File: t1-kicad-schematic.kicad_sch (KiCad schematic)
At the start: 7 parts, among them SW1 SW_MEC_5G, SW2 SW_MEC_5G, U1 Keypad

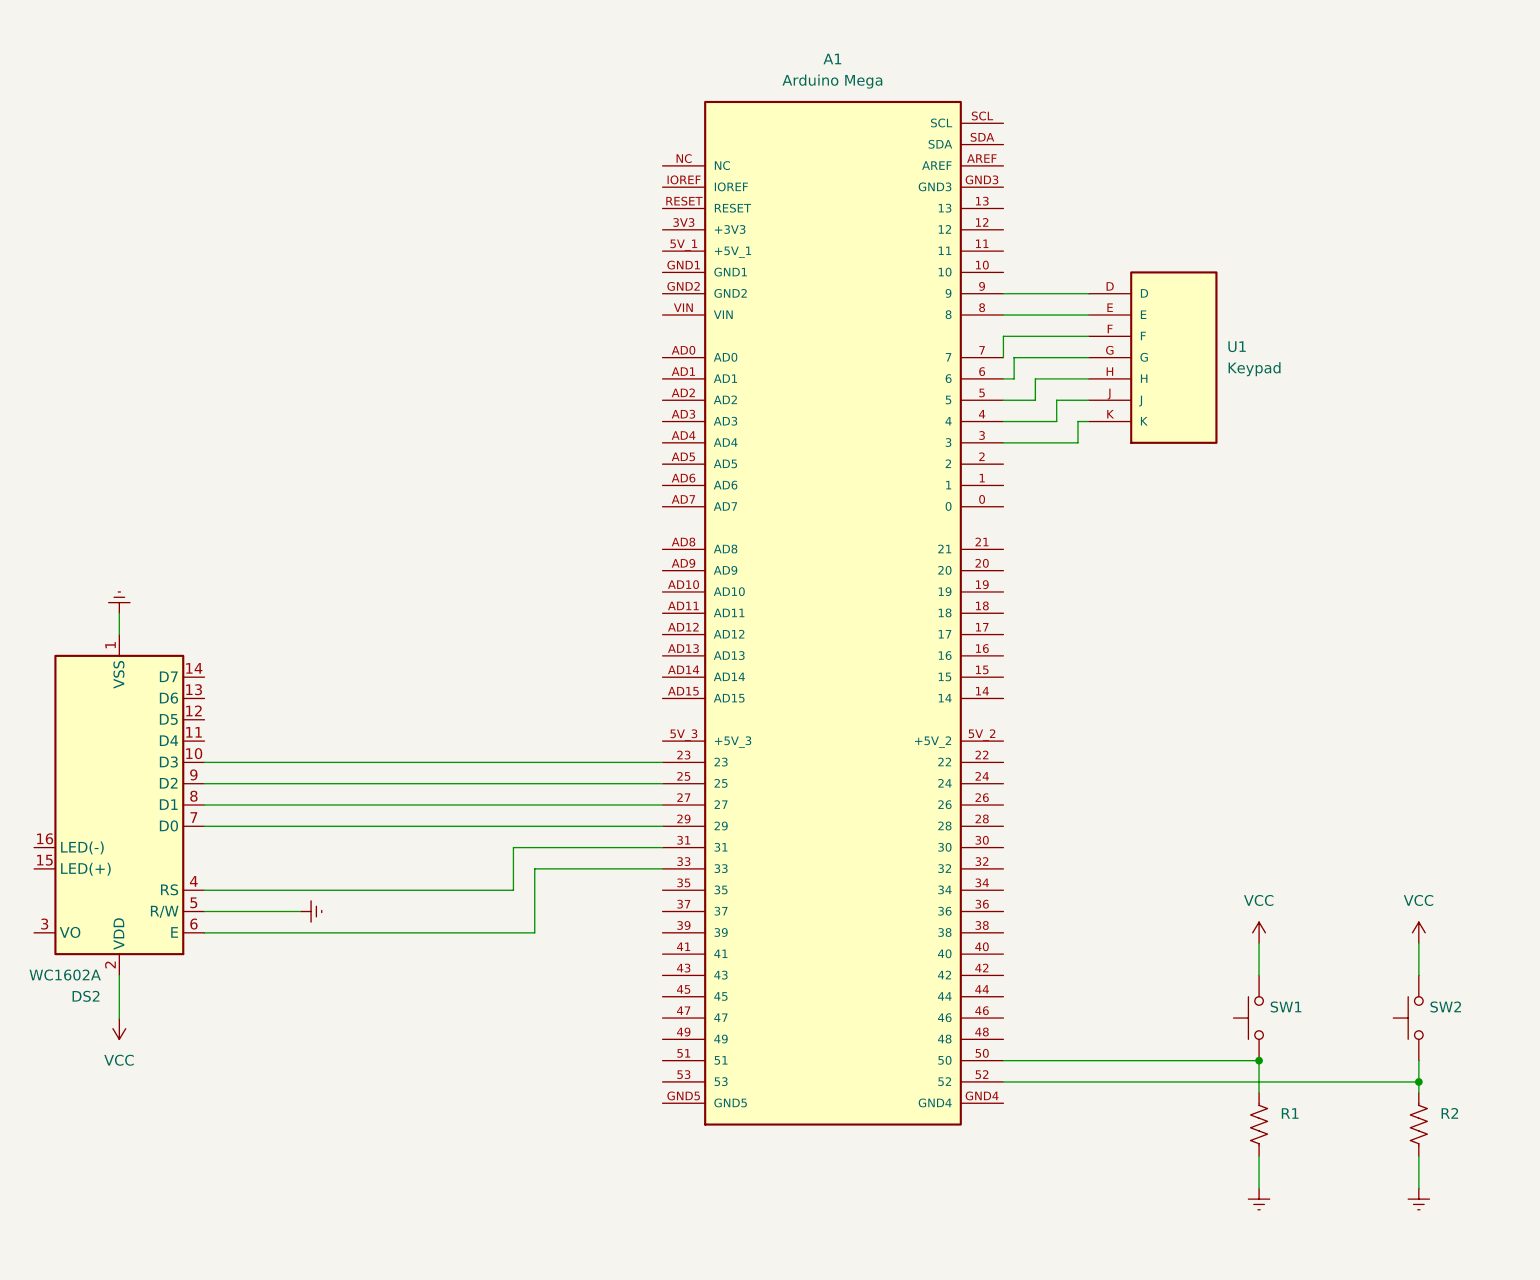
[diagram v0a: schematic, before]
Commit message: update schematic
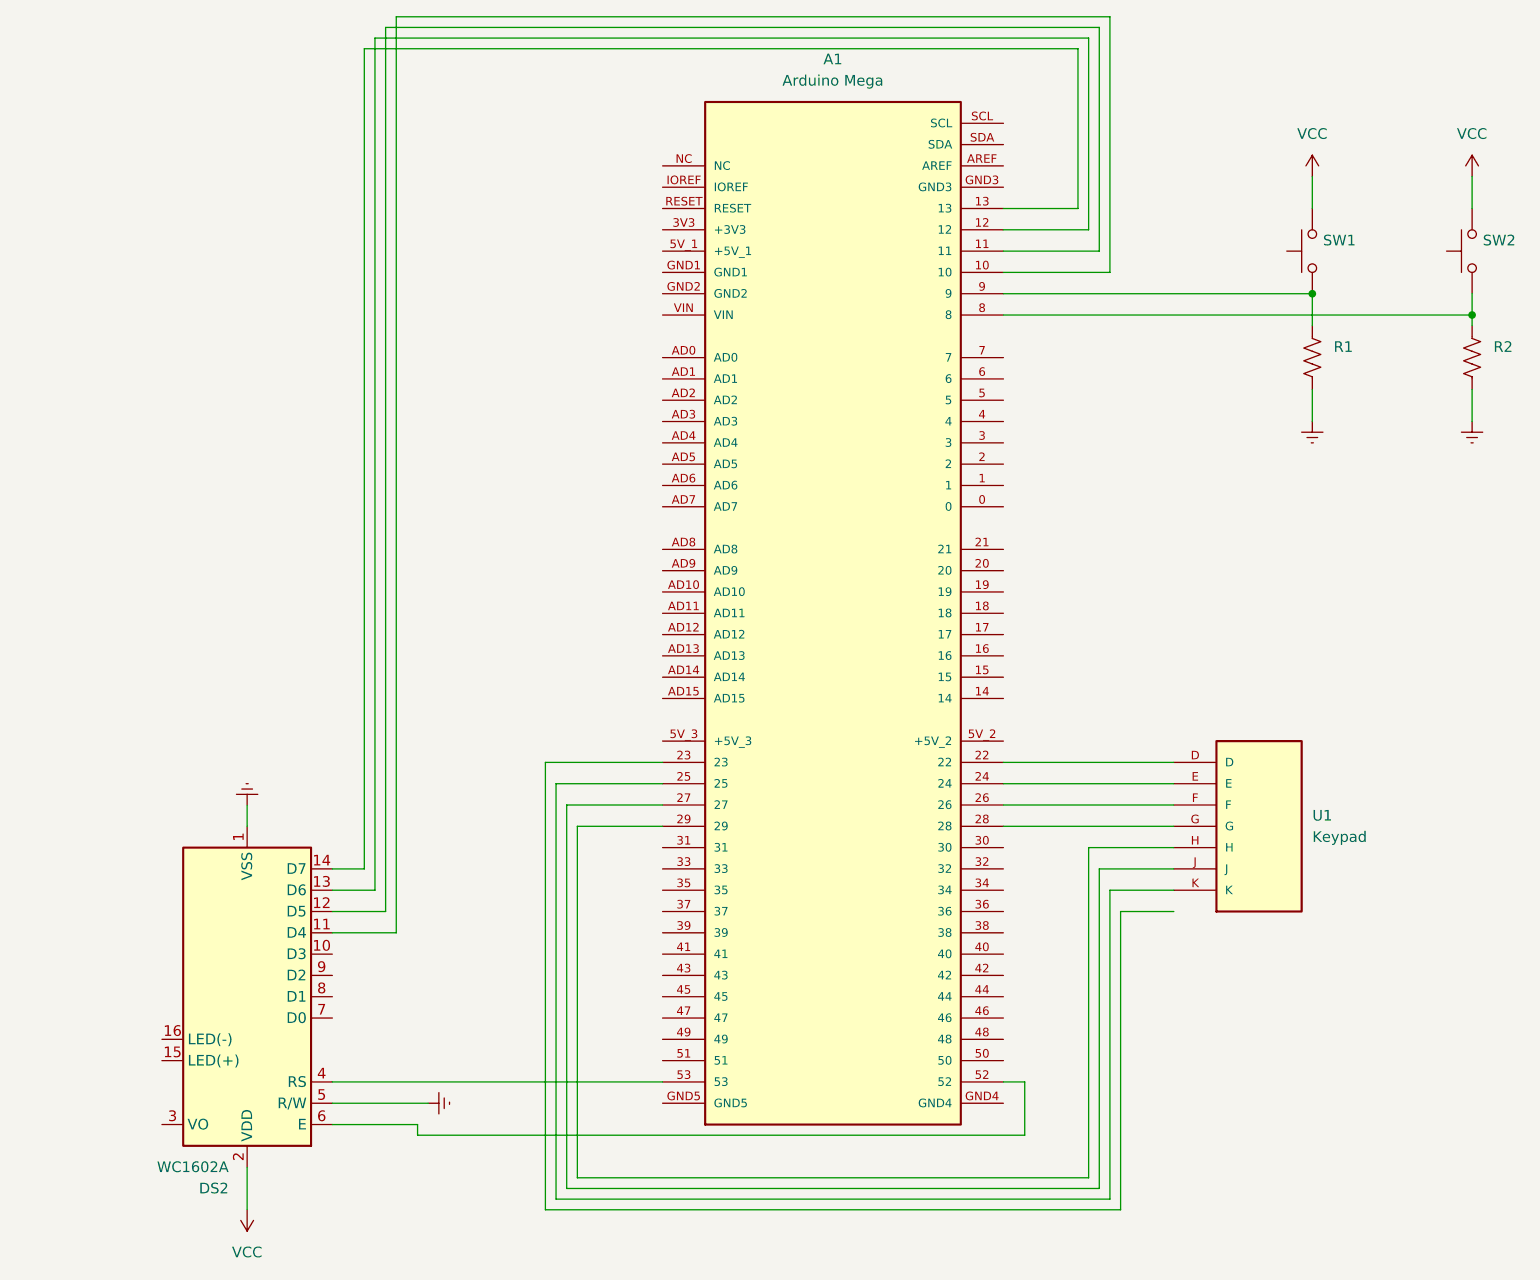
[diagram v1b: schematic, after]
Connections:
- net at R1.2, SW1.1 (A), SW1.2 (A): now also A1.9; no longer A1.50
- net at A1.10: now also DS2.11 (D4)
- net at A1.11: now also DS2.12 (D5)
- net at A1.12: now also DS2.13 (D6)
- net at A1.13: now also DS2.14 (D7)
- net at A1.22: now also U1.D
- net at A1.23: no longer DS2.10 (D3)
- net at A1.24: now also U1.E
- net at A1.25: now also U1.K; no longer DS2.9 (D2)
- net at A1.26: now also U1.F
- net at A1.27: now also U1.J; no longer DS2.8 (D1)
- net at A1.28: now also U1.G
- net at A1.29: now also U1.H; no longer DS2.7 (D0)
- net at A1.3: no longer U1.K
- net at A1.31: no longer DS2.4 (RS)
- net at A1.33: no longer DS2.6 (E)
- net at A1.4: no longer U1.J
- net at A1.5: no longer U1.H
- net at R2.2, SW2.1 (A), SW2.2 (A): now also A1.8; no longer A1.52
- net at A1.53: now also DS2.4 (RS)
- net at A1.6: no longer U1.G
- net at A1.7: no longer U1.F
- new net: A1.52, DS2.6 (E)
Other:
- moved on the sheet: DS2, R1, R2, SW1, SW2, U1
